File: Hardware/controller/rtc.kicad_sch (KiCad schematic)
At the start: 7 parts

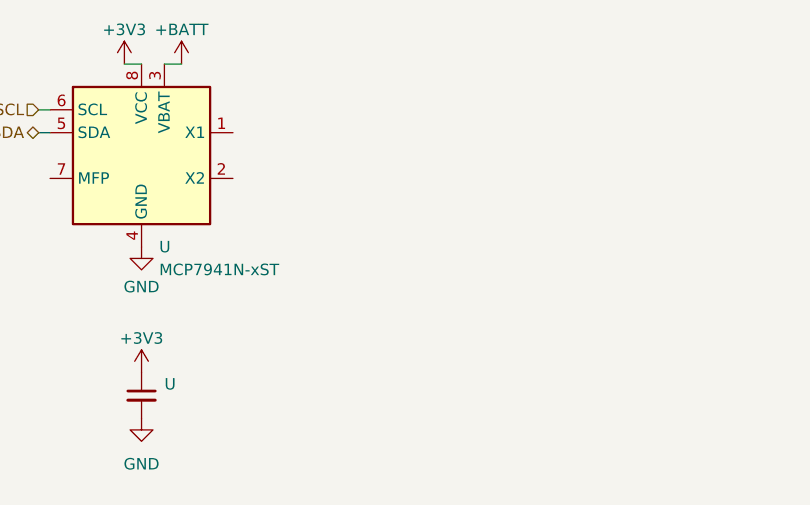
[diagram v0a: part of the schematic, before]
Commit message: hw: add RTC oscillator
- Added the RTC 32.768 kHz oscillator + capacitors to the board for the
  i2c RTC
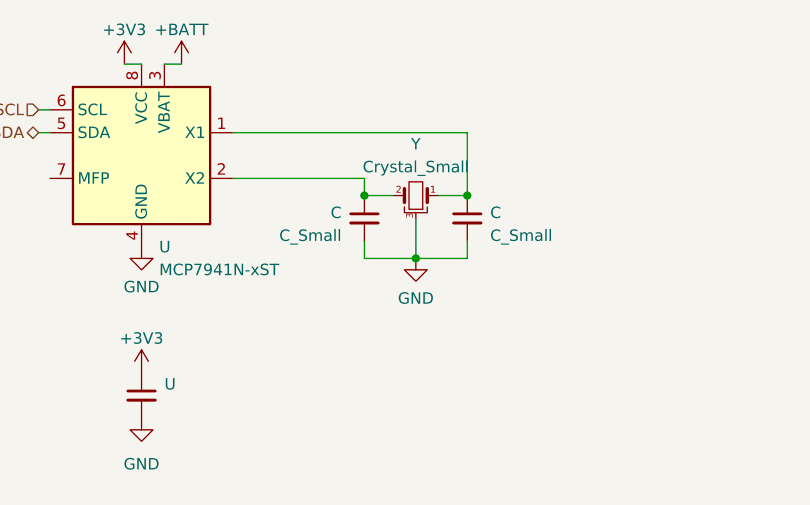
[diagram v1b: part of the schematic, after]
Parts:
- added C (x2): C_Small, symbol Device:C_Small
- added Y: Crystal_Small, symbol Device:Crystal_GND3_Small
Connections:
- net GND: now also C.2, C.2, Y.3
- net at U.1 (X1): now also C.1, Y.1
- net at U.2 (X2): now also C.1, Y.2
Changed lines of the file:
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@@
   (junction (at 158.115 80.645) (diameter 0) (color 0 0 0 0)
   )
+  (junction (at 75.565 43.815) (diameter 0) (color 0 0 0 0)
+  )
+  (junction (at 64.135 43.815) (diameter 0) (color 0 0 0 0)
+  )
+  (junction (at 69.85 50.8) (diameter 0) (color 0 0 0 0)
+  )
   (junction (at 140.97 80.645) (diameter 0) (color 0 0 0 0)
   )
+  (wire (pts (xy 49.53 36.83) (xy 75.565 36.83))
+    (stroke (width 0) (type default))
+  )
   (wire (pts (xy 158.115 80.645) (xy 158.115 81.915))
     (stroke (width 0) (type default))
@@
     (stroke (width 0) (type default))
   )
+  (wire (pts (xy 75.565 50.8) (xy 75.565 48.895))
+    (stroke (width 0) (type default))
+  )
   (wire (pts (xy 140.97 88.265) (xy 158.115 88.265))
     (stroke (width 0) (type default))
   )
+  (wire (pts (xy 72.39 43.815) (xy 75.565 43.815))
+    (stroke (width 0) (type default))
+  )
   (wire (pts (xy 139.065 80.645) (xy 140.97 80.645))
     (stroke (width 0) (type default))
@@
     (stroke (width 0) (type default))
   )
+  (wire (pts (xy 49.53 41.91) (xy 64.135 41.91))
+    (stroke (width 0) (type default))
+  )
+  (wire (pts (xy 64.135 50.8) (xy 69.85 50.8))
+    (stroke (width 0) (type default))
+  )
+  (wire (pts (xy 69.85 46.355) (xy 69.85 50.8))
+    (stroke (width 0) (type default))
+  )
+  (wire (pts (xy 69.85 50.8) (xy 75.565 50.8))
+    (stroke (width 0) (type default))
+  )
   (wire (pts (xy 140.97 80.645) (xy 158.115 80.645))
     (stroke (width 0) (type default))
   )
+  (wire (pts (xy 64.135 48.895) (xy 64.135 50.8))
+    (stroke (width 0) (type default))
+  )
+  (wire (pts (xy 75.565 36.83) (xy 75.565 43.815))
+    (stroke (width 0) (type default))
+  )
+  (wire (pts (xy 64.135 43.815) (xy 67.31 43.815))
+    (stroke (width 0) (type default))
+  )
   (wire (pts (xy 41.91 29.21) (xy 43.815 29.21))
     (stroke (width 0) (type default))
   )
   (wire (pts (xy 131.445 80.645) (xy 133.985 80.645))
+    (stroke (width 0) (type default))
+  )
+  (wire (pts (xy 64.135 41.91) (xy 64.135 43.815))
     (stroke (width 0) (type default))
   )
@@
     )
     (property "Datasheet" "~" (id 3) (at 140.97 80.645 0)
+      (effects (font (size 1.27 1.27)) hide)
+    )
+    (pin "1")
+  )
+  (symbol (lib_id "power:GND") (at 69.85 50.8 0) (unit 1)
+    (in_bom yes) (on_board yes)
+    (default_instance (reference "#PWR") (unit 1) (value "GND") (footprint ""))
+    (property "Reference" "#PWR" (id 0) (at 69.85 57.15 0)
+      (effects (font (size 1.27 1.27)) hide)
+    )
+    (property "Value" "GND" (id 1) (at 69.85 55.245 0)
+      (effects (font (size 1.27 1.27)))
+    )
+    (property "Footprint" "" (id 2) (at 69.85 50.8 0)
+      (effects (font (size 1.27 1.27)) hide)
+    )
+    (property "Datasheet" "" (id 3) (at 69.85 50.8 0)
       (effects (font (size 1.27 1.27)) hide)
     )
@@
     (pin "2")
   )
+  (symbol (lib_id "Device:C_Small") (at 64.135 46.355 0) (mirror y) (unit 1)
+    (in_bom yes) (on_board yes)
+    (default_instance (reference "C") (unit 1) (value "C_Small") (footprint ""))
+    (property "Reference" "C" (id 0) (at 61.595 45.7263 0)
+      (effects (font (size 1.27 1.27)) (justify left))
+    )
+    (property "Value" "C_Small" (id 1) (at 61.595 48.2663 0)
+      (effects (font (size 1.27 1.27)) (justify left))
+    )
+    (property "Footprint" "" (id 2) (at 64.135 46.355 0)
+      (effects (font (size 1.27 1.27)) hide)
+    )
+    (property "Datasheet" "~" (id 3) (at 64.135 46.355 0)
+      (effects (font (size 1.27 1.27)) hide)
+    )
+    (property "JLCPCB" "C1679" (id 4) (at 64.135 46.355 0)
+      (effects (font (size 1.27 1.27)) hide)
+    )
+    (pin "1")
+    (pin "2")
+  )
+  (symbol (lib_id "Device:Crystal_GND3_Small") (at 69.85 43.815 0) (mirror y) (unit 1)
+    (in_bom yes) (on_board yes)
+    (default_instance (reference "Y") (unit 1) (value "Crystal_Small") (footprint ""))
+    (property "Reference" "Y" (id 0) (at 69.85 38.1 0)
+      (effects (font (size 1.27 1.27)))
+    )
+    (property "Value" "Crystal_Small" (id 1) (at 69.85 40.64 0)
+      (effects (font (size 1.27 1.27)))
+    )
+    (property "Footprint" "" (id 2) (at 69.85 43.815 0)
+      (effects (font (size 1.27 1.27)) hide)
+    )
+    (property "Datasheet" "~" (id 3) (at 69.85 43.815 0)
+      (effects (font (size 1.27 1.27)) hide)
+    )
+    (property "MPN" "AB26T-32.768KHZ-6-B" (id 5) (at 69.85 43.815 0)
+      (effects (font (size 1.27 1.27)) hide)
+    )
+    (pin "1")
+    (pin "2")
+    (pin "3")
+  )
   (symbol (lib_id "power:GND") (at 140.97 88.265 0) (unit 1)
     (in_bom yes) (on_board yes) (fields_autoplaced)
@@
       (effects (font (size 1.27 1.27)) hide)
     )
+    (pin "1")
+    (pin "2")
+  )
+  (symbol (lib_id "Device:C_Small") (at 75.565 46.355 0) (unit 1)
+    (in_bom yes) (on_board yes) (fields_autoplaced)
+    (default_instance (reference "C") (unit 1) (value "C_Small") (footprint ""))
+    (property "Reference" "C" (id 0) (at 78.105 45.7263 0)
+      (effects (font (size 1.27 1.27)) (justify left))
+    )
+    (property "Value" "C_Small" (id 1) (at 78.105 48.2663 0)
+      (effects (font (size 1.27 1.27)) (justify left))
+    )
+    (property "Footprint" "" (id 2) (at 75.565 46.355 0)
+      (effects (font (size 1.27 1.27)) hide)
+    )
+    (property "Datasheet" "~" (id 3) (at 75.565 46.355 0)
+      (effects (font (size 1.27 1.27)) hide)
+    )
+    (property "JLCPCB" "C1679" (id 4) (at 75.565 46.355 0)
+      (effects (font (size 1.27 1.27)) hide)
+    )

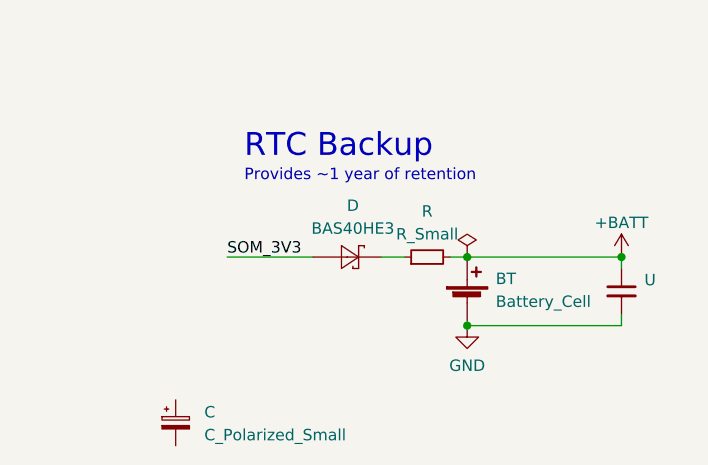
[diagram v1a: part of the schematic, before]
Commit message: hw: updates to usb host connector
- added a status indicator LED (including a lightpipe) next to the host
  connector

- start reworking the host connector power arrangement, using an actual
  USB power switch + current limiting IC (though we should revisit
  whether we'll use one without an error output)

- create footprint for AP22817 USB power switch
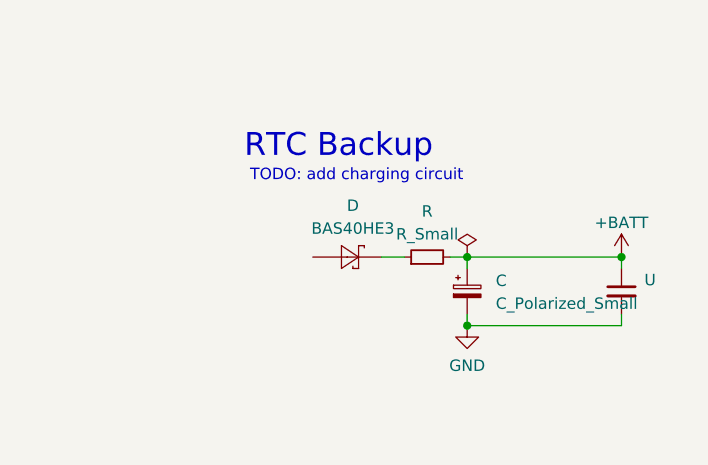
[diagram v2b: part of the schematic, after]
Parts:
- removed BT: Battery_Cell, symbol Device:Battery_Cell
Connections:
- net +BATT: now also C.1
- net GND: now also C.2
- net SOM_3V3: no longer names the net of D.1
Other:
- note added: "TODO: add charging circuit"
- note removed: "Provides ~1 year of retention"
- moved on the sheet: C
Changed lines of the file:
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@@
     (rev "4")
   )
+  (junction (at 158.115 80.645) (diameter 0) (color 0 0 0 0)
+  )
   (junction (at 140.97 88.265) (diameter 0) (color 0 0 0 0)
   )
-  (junction (at 158.115 80.645) (diameter 0) (color 0 0 0 0)
-  )
   (junction (at 75.565 43.815) (diameter 0) (color 0 0 0 0)
   )
@@
     (stroke (width 0) (type default))
   )
+  (wire (pts (xy 140.97 86.995) (xy 140.97 88.265))
+    (stroke (width 0) (type default))
+  )
   (wire (pts (xy 37.465 29.21) (xy 39.37 29.21))
     (stroke (width 0) (type default))
@@
     (stroke (width 0) (type default))
   )
+  (wire (pts (xy 140.97 80.645) (xy 140.97 81.915))
+    (stroke (width 0) (type default))
+  )
   (wire (pts (xy 69.85 46.355) (xy 69.85 50.8))
     (stroke (width 0) (type default))
@@
     (stroke (width 0) (type default))
   )
-  (wire (pts (xy 114.3 80.645) (xy 123.825 80.645))
-    (stroke (width 0) (type default))
-  )
   (wire (pts (xy 27.94 36.83) (xy 29.21 36.83))
     (stroke (width 0) (type default))
+  )
+  (text "TODO: add charging circuit" (at 116.84 72.39 0)
+    (effects (font (size 1.27 1.27)) (justify left bottom))
   )
   (text "RTC Backup" (at 116.205 69.85 0)
     (effects (font (size 2.54 2.54)) (justify left bottom))
-  )
-  (text "Provides ~1 year of retention" (at 116.205 72.39 0)
-    (effects (font (size 1.27 1.27)) (justify left bottom))
-  )
-  (label "SOM_3V3" (at 114.3 80.645 0) (fields_autoplaced)
-    (effects (font (size 1.27 1.27)) (justify left bottom))
   )
   (hierarchical_label "I²C_SDA" (shape bidirectional) (at 27.94 36.83 180) (fields_autoplaced)
@@
     (pin "8")
   )
-  (symbol (lib_id "Device:Battery_Cell") (at 140.97 85.725 0) (unit 1)
-    (in_bom yes) (on_board yes) (fields_autoplaced)
-    (default_instance (reference "BT") (unit 1) (value "Battery_Cell") (footprint ""))
-    (property "Reference" "BT" (id 0) (at 144.145 83.058 0)
-      (effects (font (size 1.27 1.27)) (justify left))
-    )
-    (property "Value" "Battery_Cell" (id 1) (at 144.145 85.598 0)
-      (effects (font (size 1.27 1.27)) (justify left))
-    )
-    (property "Footprint" "" (id 2) (at 140.97 84.201 90)
-      (effects (font (size 1.27 1.27)) hide)
-    )
-    (property "Datasheet" "~" (id 3) (at 140.97 84.201 90)
-      (effects (font (size 1.27 1.27)) hide)
-    )
-    (property "MPN" "ML-1220/V1AN" (id 4) (at 140.97 85.725 0)
-      (effects (font (size 1.27 1.27)) hide)
-    )
-    (pin "1")
-    (pin "2")
-  )
   (symbol (lib_id "power:+3V3") (at 37.465 29.21 0) (unit 1)
     (in_bom yes) (on_board yes) (fields_autoplaced)
@@
     (pin "2")
   )
-  (symbol (lib_id "Device:C_Polarized_Small") (at 108.585 99.06 0) (unit 1)
+  (symbol (lib_id "Device:C_Polarized_Small") (at 140.97 84.455 0) (unit 1)
     (in_bom yes) (on_board yes) (fields_autoplaced)
     (default_instance (reference "C") (unit 1) (value "C_Polarized_Small") (footprint ""))
-    (property "Reference" "C" (id 0) (at 111.76 97.8789 0)
-      (effects (font (size 1.27 1.27)) (justify left))
-    )
-    (property "Value" "C_Polarized_Small" (id 1) (at 111.76 100.4189 0)
-      (effects (font (size 1.27 1.27)) (justify left))
-    )
-    (property "Footprint" "" (id 2) (at 108.585 99.06 0)
-      (effects (font (size 1.27 1.27)) hide)
-    )
-    (property "Datasheet" "~" (id 3) (at 108.585 99.06 0)
-      (effects (font (size 1.27 1.27)) hide)
-    )
+    (property "Reference" "C" (id 0) (at 144.145 83.2739 0)
+      (effects (font (size 1.27 1.27)) (justify left))
+    )
+    (property "Value" "C_Polarized_Small" (id 1) (at 144.145 85.8139 0)
+      (effects (font (size 1.27 1.27)) (justify left))
+    )
+    (property "Footprint" "" (id 2) (at 140.97 84.455 0)
+      (effects (font (size 1.27 1.27)) hide)
+    )
+    (property "Datasheet" "~" (id 3) (at 140.97 84.455 0)
+      (effects (font (size 1.27 1.27)) hide)
+    )

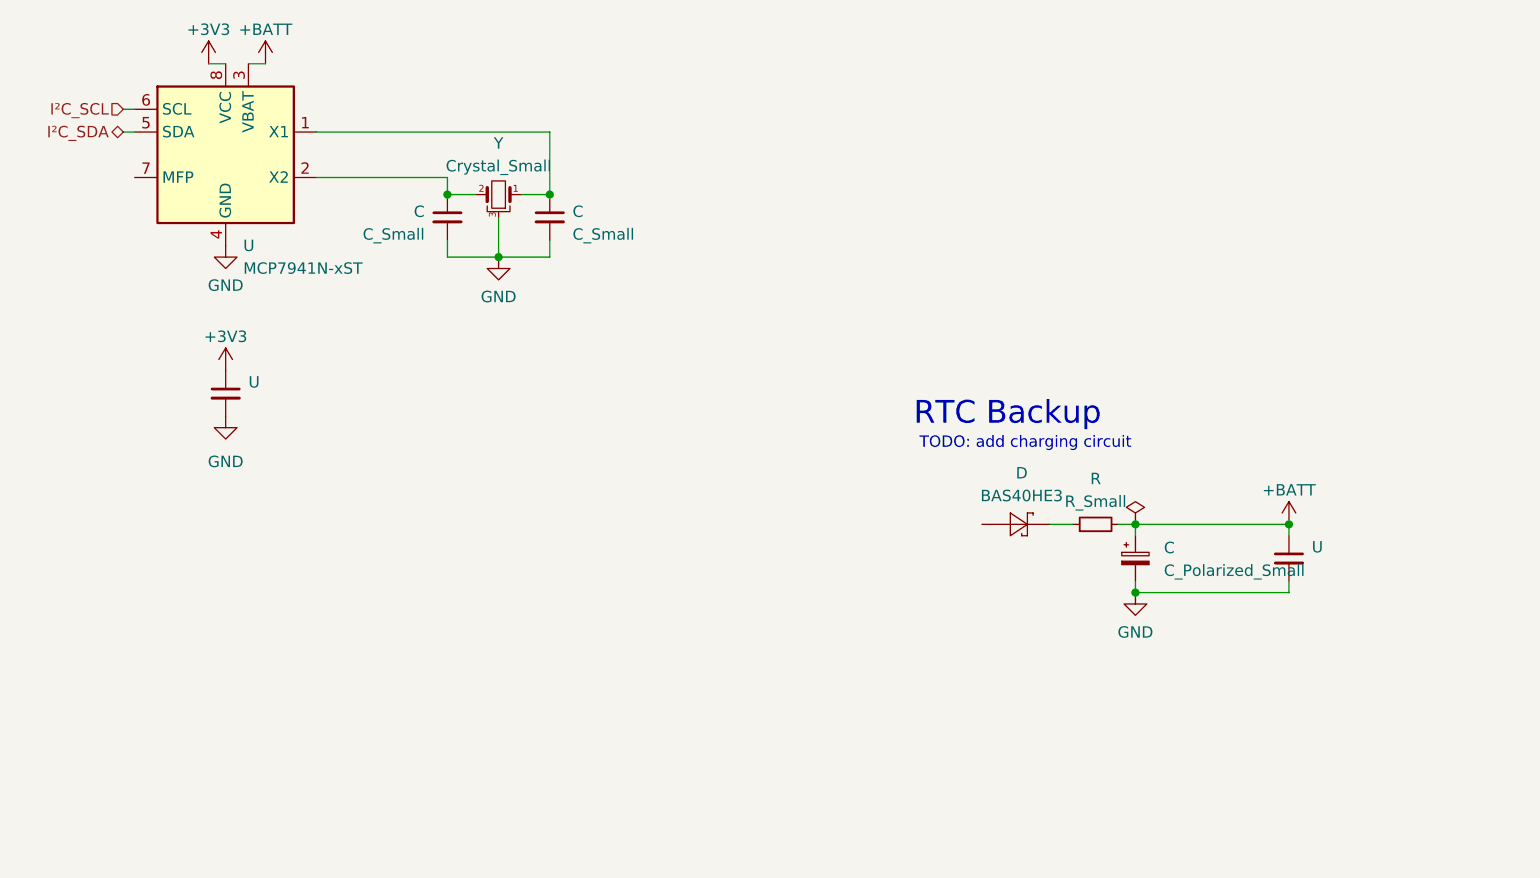
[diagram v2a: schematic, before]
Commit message: hw: add charger for RTC
- added RTC supercapacitor

- added the charging circuit for the RTC (with adjustment for voltage
  and all that fun stuff) based around a bonus linear regulator for the
  supercap

- minor tweaks all around: add more JLCPCB part numbers and fixed some
  footprints for some components
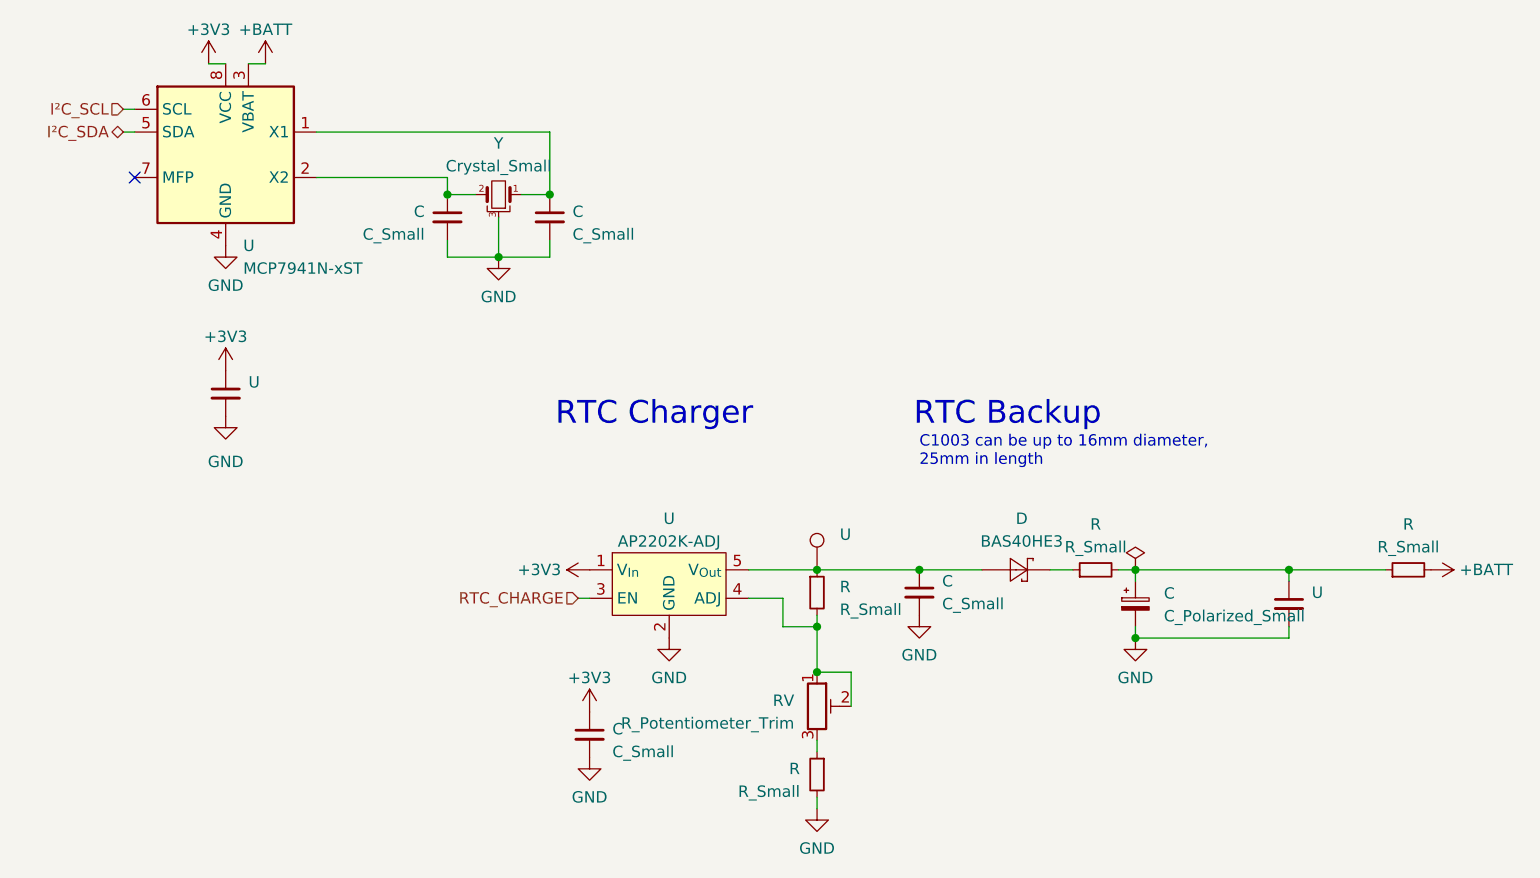
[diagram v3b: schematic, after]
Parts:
- added C (x2): C_Small, symbol Device:C_Small
- added R (x3): R_Small, symbol Device:R_Small
- added RV: R_Potentiometer_Trim, symbol Device:R_Potentiometer_Trim
- added U: (no value), symbol Connector:TestPoint
- added U: AP2202K-ADJ, Package_TO_SOT_SMD:SOT-23-5_HandSoldering, symbol programmable-load:AP2202K-ADJ
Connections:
- net +3V3: now also C.1, U.1 (V_{In})
- net +BATT: now also R.2; no longer C.1, R.2, U.1
- net GND: now also C.2, C.2, R.2, U.2 (GND)
- net at D.1: now also C.1, R.1, U.1, U.5 (V_{Out})
- new net: R.2, RV.1, RV.2, U.4 (ADJ)
- new net: R.1, RV.3
- new net: C.1, R.1, R.2, U.1
- new net RTC_CHARGE: U.3 (EN)
- no-connect marks 0 -> 1
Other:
- note added: "C1003 can be up to 16mm diameter, 25mm in length"
- note added: "RTC Charger"
- note removed: "TODO: add charging circuit"
- moved on the sheet: C, D, R, U

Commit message: hw: add more jlcpcb p/n; minor cleanup
- added jlcpcb part numbers for various resistors and passives

- minor clean up of stuff on the board, including moving the +VDC
  indicator LED and widening the fastener slot for the RTC supercap
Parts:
- R: JLCPCB (none) -> C23138
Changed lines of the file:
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@@
+      (effects (font (size 1.27 1.27)) hide)
+    )
+    (property "JLCPCB" "C23138" (id 5) (at 171.45 85.725 90)
       (effects (font (size 1.27 1.27)) hide)
     )
@@
       (effects (font (size 1.27 1.27)) hide)
     )
+    (property "JLCPCB" "C23138" (id 5) (at 136.525 85.725 90)
+      (effects (font (size 1.27 1.27)) hide)
+    )

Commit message: hw: add more part numbers, cleanup
- Added JLCPCB part numbers for more passive components

- Added a status LED for the rear of the board (next to the device USB
  port)
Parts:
- C: JLCPCB (none) -> C15849
- U: JLCPCB (none) -> C14663
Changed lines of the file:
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@@
   (junction (at 105.41 85.725) (diameter 0) (color 0 0 0 0)
+  )
+  (junction (at 173.99 85.725) (diameter 0) (color 0 0 0 0)
   )
   (junction (at 140.97 85.725) (diameter 0) (color 0 0 0 0)
@@
       (effects (font (size 1.27 1.27)) hide)
     )
+    (property "JLCPCB" "C15849" (id 5) (at 80.01 104.14 0)
+      (effects (font (size 1.27 1.27)) hide)
+    )
     (pin "1")
     (pin "2")
@@
     (pin "1")
   )
-  (symbol (lib_id "power:PWR_FLAG") (at 140.97 85.725 0) (unit 1)
+  (symbol (lib_id "power:PWR_FLAG") (at 173.99 85.725 180) (unit 1)
     (in_bom yes) (on_board yes) (fields_autoplaced)
     (default_instance (reference "#FLG") (unit 1) (value "PWR_FLAG") (footprint ""))
-    (property "Reference" "#FLG" (id 0) (at 140.97 83.82 0)
-      (effects (font (size 1.27 1.27)) hide)
-    )
-    (property "Value" "PWR_FLAG" (id 1) (at 140.97 82.55 0)
-      (effects (font (size 1.27 1.27)) hide)
-    )
-    (property "Footprint" "" (id 2) (at 140.97 85.725 0)
-      (effects (font (size 1.27 1.27)) hide)
-    )
-    (property "Datasheet" "~" (id 3) (at 140.97 85.725 0)
+    (property "Reference" "#FLG" (id 0) (at 173.99 87.63 0)
+      (effects (font (size 1.27 1.27)) hide)
+    )
+    (property "Value" "PWR_FLAG" (id 1) (at 173.99 88.9 0)
+      (effects (font (size 1.27 1.27)) hide)
+    )
+    (property "Footprint" "" (id 2) (at 173.99 85.725 0)
+      (effects (font (size 1.27 1.27)) hide)
+    )
+    (property "Datasheet" "~" (id 3) (at 173.99 85.725 0)
       (effects (font (size 1.27 1.27)) hide)
     )
@@
       (effects (font (size 1.27 1.27)) hide)
     )
+    (property "JLCPCB" "C14663" (id 5) (at 158.115 89.535 0)
+      (effects (font (size 1.27 1.27)) hide)
+    )
     (pin "1")
     (pin "2")
@@
       (effects (font (size 1.27 1.27)) hide)
     )
+    (property "JLCPCB" "C14663" (id 5) (at 39.37 66.04 0)
+      (effects (font (size 1.27 1.27)) hide)
+    )
